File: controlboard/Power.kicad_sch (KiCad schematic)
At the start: 35 parts, among them J11 Pololu Voltage Regulator, J4 USB_C_Receptacle_USB2.0_14P, J7 Screw_Terminal_01x02, J9 mini560 voltage regulator, Q2 PMOS AO3401A, U4 CH224K

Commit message: progress
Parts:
- removed JP25: SolderJumper_2_Bridged, Jumper:SolderJumper-2_P1.3mm_Bridged2Bar_RoundedPad1.0x1.5mm, symbol Jumper:SolderJumper_2_Bridged
- TP6: footprint Connector_PinSocket_2.54mm:PinSocket_1x01_P2.54mm_Vertical -> TestPoint:TestPoint_THTPad_1.5x1.5mm_Drill0.7mm
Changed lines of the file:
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@@
 	(wire
 		(pts
-			(xy 88.9 31.75) (xy 86.36 31.75)
-		)
-		(stroke
-			(width 0)
-			(type default)
-		)
-	)
-	(wire
-		(pts
 			(xy 93.98 114.3) (xy 107.95 114.3)
 		)
@@
 	(wire
 		(pts
-			(xy 96.52 31.75) (xy 99.06 31.75)
-		)
-		(stroke
-			(width 0)
-			(type default)
-		)
-	)
-	(wire
-		(pts
 			(xy 245.11 144.78) (xy 245.11 143.51)
 		)
@@
 	(wire
 		(pts
-			(xy 99.06 31.75) (xy 99.06 40.64)
-		)
-		(stroke
-			(width 0)
-			(type default)
-		)
-	)
-	(wire
-		(pts
 			(xy 92.71 49.53) (xy 83.82 49.53)
 		)
@@
 	(wire
 		(pts
-			(xy 86.36 31.75) (xy 86.36 40.64)
-		)
-		(stroke
-			(width 0)
-			(type default)
-		)
-	)
-	(wire
-		(pts
 			(xy 46.99 19.05) (xy 48.26 19.05)
 		)
@@
 	(wire
 		(pts
+			(xy 86.36 36.83) (xy 86.36 40.64)
+		)
+		(stroke
+			(width 0)
+			(type default)
+		)
+	)
+	(wire
+		(pts
 			(xy 55.88 38.1) (xy 55.88 35.56)
 		)
@@
 	)
 	(symbol
-		(lib_id "Jumper:SolderJumper_2_Bridged")
-		(at 92.71 31.75 0)
-		(unit 1)
-		(exclude_from_sim yes)
-		(in_bom no)
-		(on_board yes)
-		(dnp no)
-		(property "Reference" "JP25"
-			(at 96.266 30.734 0)
-			(effects
-				(font
-					(size 1.27 1.27)
-				)
-			)
-		)
-		(property "Value" "SolderJumper_2_Bridged"
-			(at 92.71 27.94 0)
-			(effects
-				(font
-					(size 1.27 1.27)
-				)
-				(hide yes)
-			)
-		)
-		(property "Footprint" "Jumper:SolderJumper-2_P1.3mm_Bridged2Bar_RoundedPad1.0x1.5mm"
-			(at 92.71 31.75 0)
-			(effects
-				(font
-					(size 1.27 1.27)
-				)
-				(hide yes)
-			)
-		)
-		(property "Datasheet" "~"
-			(at 92.71 31.75 0)
-			(effects
-				(font
-					(size 1.27 1.27)
-				)
-				(hide yes)
-			)
-		)
-		(property "Description" "Solder Jumper, 2-pole, closed/bridged"
-			(at 92.71 31.75 0)
-			(effects
-				(font
-					(size 1.27 1.27)
-				)
-				(hide yes)
-			)
-		)
-		(pin "1"
-		)
-		(pin "2"
-		)
-		(instances
-			(project "controlboard"
-				(path "/2797250d-6fee-4769-b4dd-0e20ce4f0941/5fab4b81-761e-4fae-b113-00364a75fd9a"
-					(reference "JP25")
-					(unit 1)
-				)
-			)
-		)
-	)
-	(symbol
 		(lib_id "Connector:TestPoint")
 		(at 267.97 135.89 0)
@@
 			)
 		)
-		(property "Footprint" "Connector_PinSocket_2.54mm:PinSocket_1x01_P2.54mm_Vertical"
+		(property "Footprint" "TestPoint:TestPoint_THTPad_1.5x1.5mm_Drill0.7mm"
 			(at 261.62 135.89 0)
 			(effects

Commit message: yay its all connected
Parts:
- TP5, TP7: footprint Connector_PinSocket_2.54mm:PinSocket_1x01_P2.54mm_Vertical -> TestPoint:TestPoint_THTPad_D2.0mm_Drill1.0mm
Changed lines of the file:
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@@
 			)
 		)
-		(property "Footprint" "Connector_PinSocket_2.54mm:PinSocket_1x01_P2.54mm_Vertical"
+		(property "Footprint" "TestPoint:TestPoint_THTPad_D2.0mm_Drill1.0mm"
 			(at 250.19 135.89 0)
 			(effects
@@
 			)
 		)
-		(property "Footprint" "Connector_PinSocket_2.54mm:PinSocket_1x01_P2.54mm_Vertical"
+		(property "Footprint" "TestPoint:TestPoint_THTPad_D2.0mm_Drill1.0mm"
 			(at 273.05 135.89 0)
 			(effects

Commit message: a
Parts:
- J4: footprint Connector_USB:USB_C_Receptacle_HRO_TYPE-C-31-M-12 -> 0chessbot-parts:USB_C_Receptacle_HRO_TYPE-C-31-M-12
- J7: footprint TerminalBlock_RND:TerminalBlock_RND_205-00287_1x02_P5.08mm_Horizontal -> TerminalBlock_Phoenix:TerminalBlock_Phoenix_PT-1,5-2-5.0-H_1x02_P5.00mm_Horizontal
- Q2: footprint Package_TO_SOT_SMD:SOT-23_Handsoldering -> Package_TO_SOT_SMD:SOT-23
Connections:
- net GND: now also J7.2 (Pin_2); no longer J7.1 (Pin_1)
- net at D29.2 (A): now also J7.1 (Pin_1); no longer J7.2 (Pin_2)
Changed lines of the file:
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@@
 			)
 		)
-		(property "Footprint" "Connector_USB:USB_C_Receptacle_HRO_TYPE-C-31-M-12"
+		(property "Footprint" "0chessbot-parts:USB_C_Receptacle_HRO_TYPE-C-31-M-12"
 			(at 35.56 45.72 0)
 			(effects
@@
 	)
 	(symbol
+		(lib_id "Connector:Screw_Terminal_01x02")
+		(at 175.26 45.72 0)
+		(mirror y)
+		(unit 1)
+		(exclude_from_sim no)
+		(in_bom yes)
+		(on_board yes)
+		(dnp no)
+		(property "Reference" "J7"
+			(at 175.26 43.18 0)
+			(effects
+				(font
+					(size 1.27 1.27)
+				)
+			)
+		)
+		(property "Value" "Screw_Terminal_01x02"
+			(at 169.418 42.926 0)
+			(effects
+				(font
+					(size 1.27 1.27)
+				)
+				(hide yes)
+			)
+		)
+		(property "Footprint" "TerminalBlock_Phoenix:TerminalBlock_Phoenix_PT-1,5-2-5.0-H_1x02_P5.00mm_Horizontal"
+			(at 175.26 45.72 0)
+			(effects
+				(font
+					(size 1.27 1.27)
+				)
+				(hide yes)
+			)
+		)
+		(property "Datasheet" "~"
+			(at 175.26 45.72 0)
+			(effects
+				(font
+					(size 1.27 1.27)
+				)
+				(hide yes)
+			)
+		)
+		(property "Description" "Generic screw terminal, single row, 01x02, script generated (kicad-library-utils/schlib/autogen/connector/)"
+			(at 175.26 45.72 0)
+			(effects
+				(font
+					(size 1.27 1.27)
+				)
+				(hide yes)
+			)
+		)
+		(pin "1"
+		)
+		(pin "2"
+		)
+		(instances
+			(project "controlboard"
+				(path "/2797250d-6fee-4769-b4dd-0e20ce4f0941/5fab4b81-761e-4fae-b113-00364a75fd9a"
+					(reference "J7")
+					(unit 1)
+				)
+			)
+		)
+	)
+	(symbol
 		(lib_id "Device:D_Schottky")
 		(at 132.08 48.26 180)
@@
 	)
 	(symbol
-		(lib_id "Connector:Screw_Terminal_01x02")
-		(at 175.26 48.26 180)
-		(unit 1)
-		(exclude_from_sim no)
-		(in_bom yes)
-		(on_board yes)
-		(dnp no)
-		(property "Reference" "J7"
-			(at 169.164 40.64 0)
-			(effects
-				(font
-					(size 1.27 1.27)
-				)
-			)
-		)
-		(property "Value" "Screw_Terminal_01x02"
-			(at 170.18 42.926 0)
-			(effects
-				(font
-					(size 1.27 1.27)
-				)
-			)
-		)
-		(property "Footprint" "TerminalBlock_RND:TerminalBlock_RND_205-00287_1x02_P5.08mm_Horizontal"
-			(at 175.26 48.26 0)
-			(effects
-				(font
-					(size 1.27 1.27)
-				)
-				(hide yes)
-			)
-		)
-		(property "Datasheet" "~"
-			(at 175.26 48.26 0)
-			(effects
-				(font
-					(size 1.27 1.27)
-				)
-				(hide yes)
-			)
-		)
-		(property "Description" "Generic screw terminal, single row, 01x02, script generated (kicad-library-utils/schlib/autogen/connector/)"
-			(at 175.26 48.26 0)
-			(effects
-				(font
-					(size 1.27 1.27)
-				)
-				(hide yes)
-			)
-		)
-		(pin "1"
-		)
-		(pin "2"
-		)
-		(instances
-			(project "controlboard"
-				(path "/2797250d-6fee-4769-b4dd-0e20ce4f0941/5fab4b81-761e-4fae-b113-00364a75fd9a"
-					(reference "J7")
-					(unit 1)
-				)
-			)
-		)
-	)
-	(symbol
 		(lib_id "Connector:Conn_01x05_Socket")
 		(at 234.95 40.64 90)
@@
 			)
 		)
-		(property "Footprint" "Package_TO_SOT_SMD:SOT-23_Handsoldering"
+		(property "Footprint" "Package_TO_SOT_SMD:SOT-23"
 			(at 118.11 43.18 0)
 			(effects

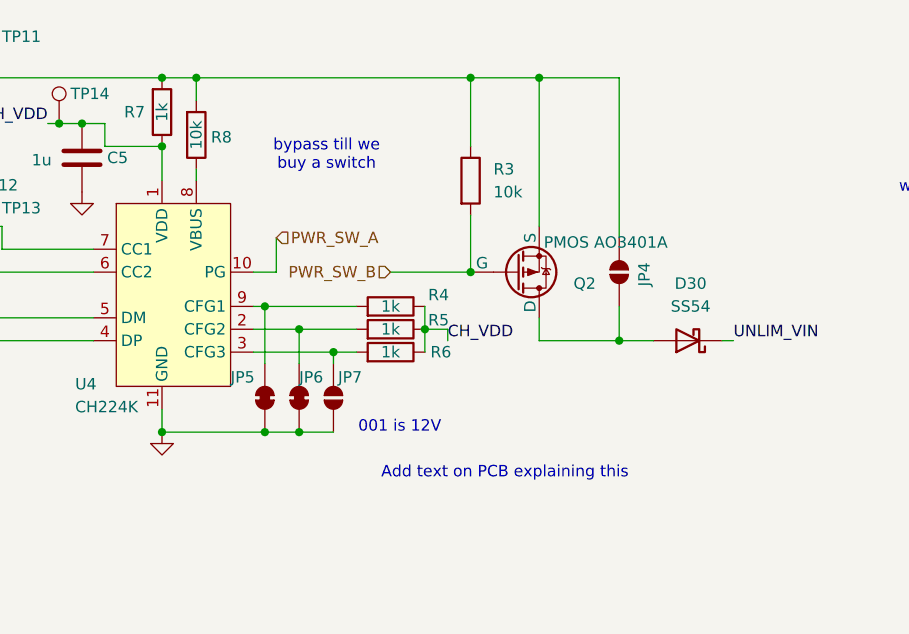
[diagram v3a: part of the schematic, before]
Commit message: controlboard: fix critical mosfet errors
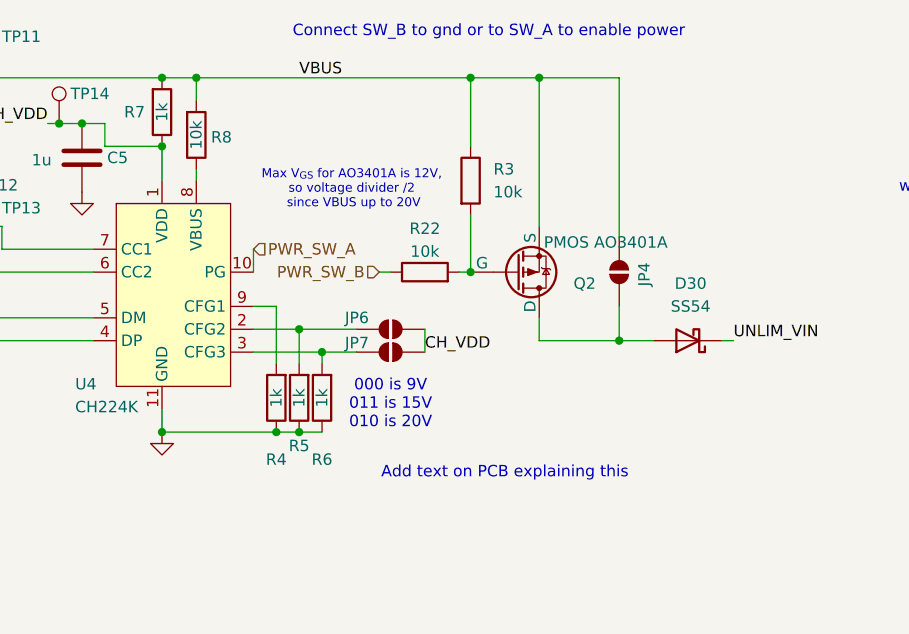
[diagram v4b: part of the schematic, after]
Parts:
- removed JP5, JP6: SolderJumper_2_Bridged, Jumper:SolderJumper-2_P1.3mm_Bridged2Bar_RoundedPad1.0x1.5mm, symbol Jumper:SolderJumper_2_Bridged
- added JP6: CFG3, Jumper:SolderJumper-2_P1.3mm_Open_RoundedPad1.0x1.5mm, symbol Jumper:SolderJumper_2_Open
- added R22: 10k, Resistor_SMD:R_0603_1608Metric_Pad0.98x0.95mm_HandSolder, symbol Device:R
- JP7: value SolderJumper_2_Open -> CFG3
- TP12, TP13: footprint TestPoint:TestPoint_THTPad_1.0x1.0mm_Drill0.5mm -> TestPoint:TestPoint_Pad_D1.0mm
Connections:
- net CH_VDD: now also JP7.1 (A), JP6.1 (A); no longer R4.1, R5.1, R6.1
- net GND: now also R4.1, R5.1, R6.1; no longer JP7.1 (A)
- net PWR_SW_B: now also R22.1; no longer Q2.2 (G), R3.2
- net VBUS: now reaches J4.A4 (VBUS), J4.A9 (VBUS), J4.B4 (VBUS), J4.B9 (VBUS), JP4.1 (A), Q2.3 (S), R3.1, R7.2, R8.2, TP11.1
- net at R5.2, U4.2 (CFG2): now also JP6.2 (B)
- new net: Q2.2 (G), R22.2, R3.2
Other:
- note added: "000 is 9V 011 is 15V 010 is 20V"
- note added: "Connect SW_B to gnd or to SW_A to enable power"
- note added: "Max V_{GS} for AO3401A is 12V, so voltage divider /2 since VBUS up to 20V"
- note removed: "001 is 12V"
- note removed: "bypass till we buy a switch"

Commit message: improvements
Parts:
- J4: value USB_C_Receptacle_USB2.0_14P -> TYPE-C-31-M-12
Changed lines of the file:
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@@
 			)
 		)
-		(property "Value" "USB_C_Receptacle_USB2.0_14P"
+		(property "Value" "TYPE-C-31-M-12"
 			(at 31.75 25.4 0)
 			(effects
@@
 			)
 		)
-		(property "RILIM" "3.6k"
+		(property "RILIM" "3k"
 			(at 78.74 133.35 0)
 			(effects

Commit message: controlboard finalized and ordered!!!
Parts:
- Q2: LCSC (none) -> AO3401A

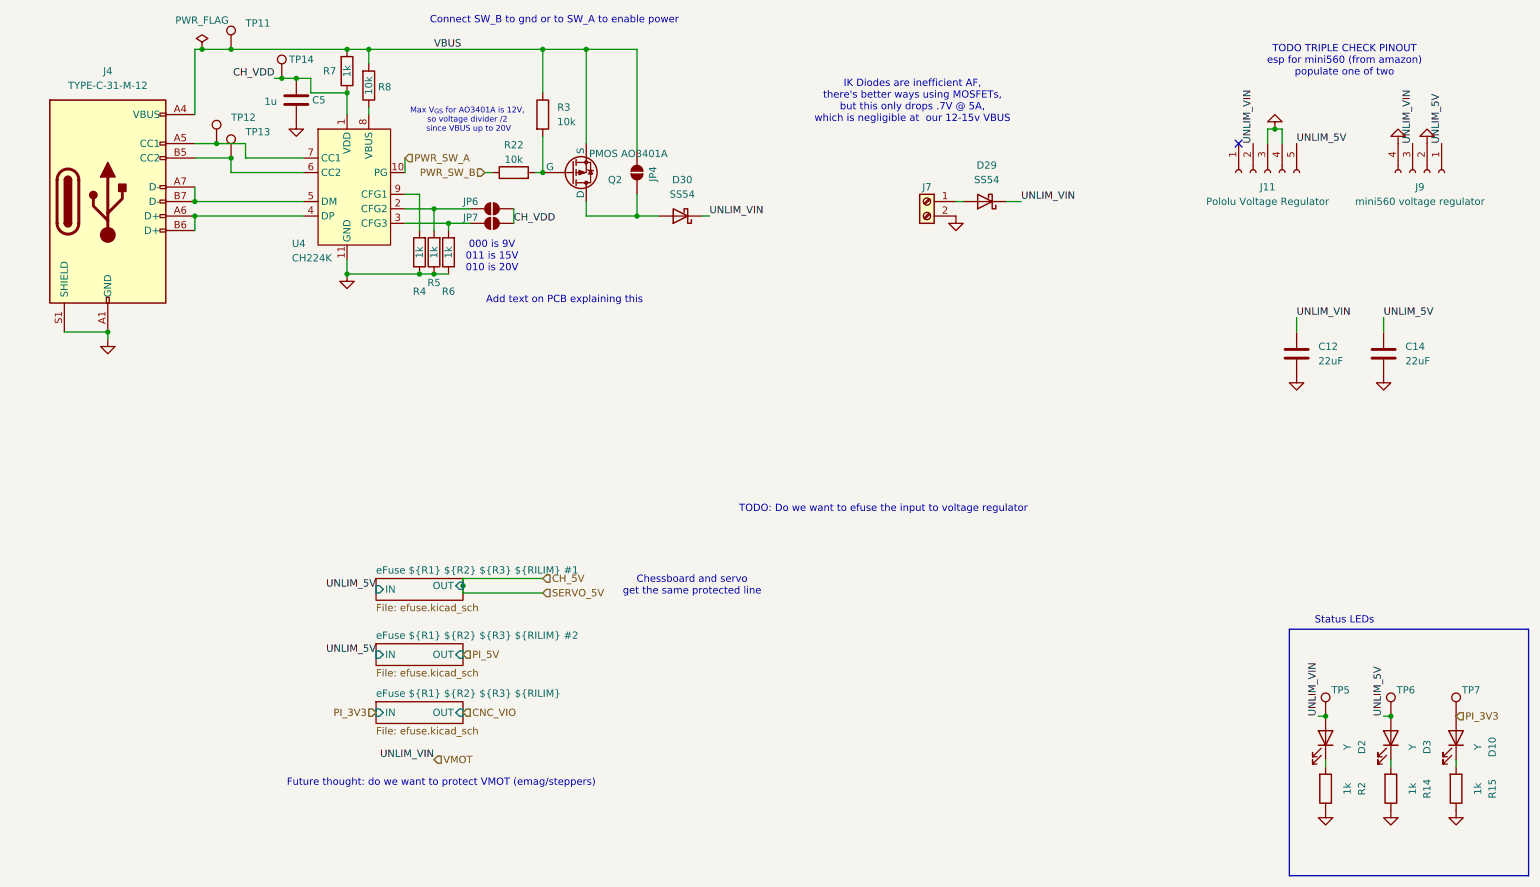
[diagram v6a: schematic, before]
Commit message: Control board changes
Made a few control board changes (green checks on discord)
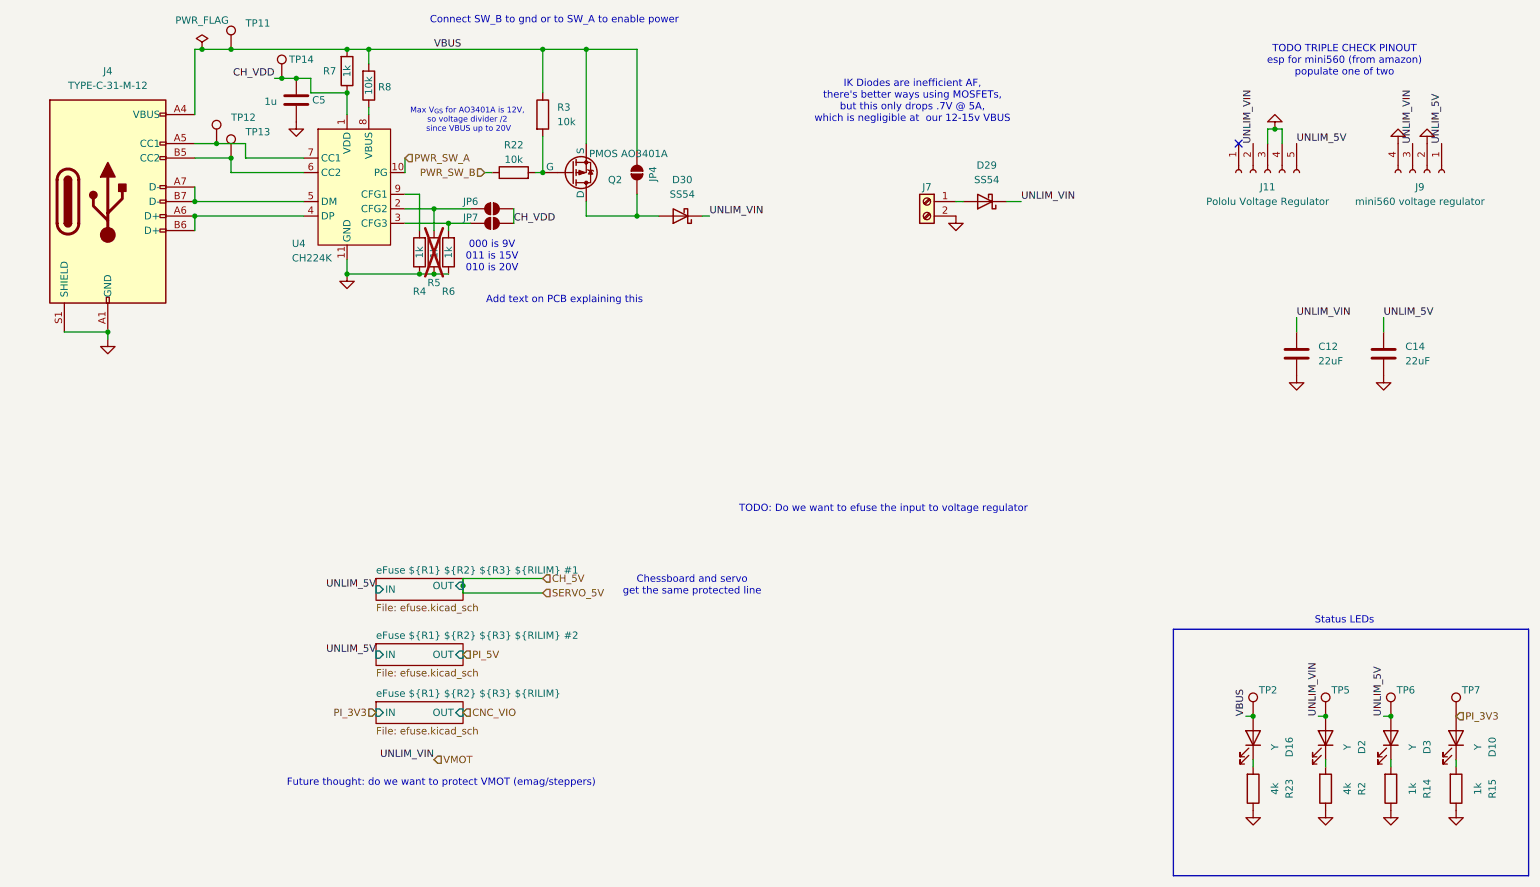
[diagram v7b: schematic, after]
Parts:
- added D16: Y, LED_SMD:LED_0603_1608Metric_Pad1.05x0.95mm_HandSolder, symbol Device:LED
- added R23: 4k, Resistor_SMD:R_0603_1608Metric_Pad0.98x0.95mm_HandSolder, symbol Device:R
- added TP2: TestPoint, TestPoint:TestPoint_THTPad_D2.0mm_Drill1.0mm, symbol Connector:TestPoint
- R2: value 1k -> 4k
- R5: now not fitted
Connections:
- net GND: now also R23.1
- net VBUS: now also D16.2 (A), TP2.1
- new net: D16.1 (K), R23.2
